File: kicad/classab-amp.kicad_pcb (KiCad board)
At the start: 2 copper layers, 116.6 x 99.3 mm, 81 parts, among them J1 INPUT, Q1 2N5401, Q10 BD140, Q11 BD139, Q12 BD139, Q13 TTC004B, Q14 TTA004B, Q15 IRFP240, Q16 IRFP9240, Q17 IRFP9240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

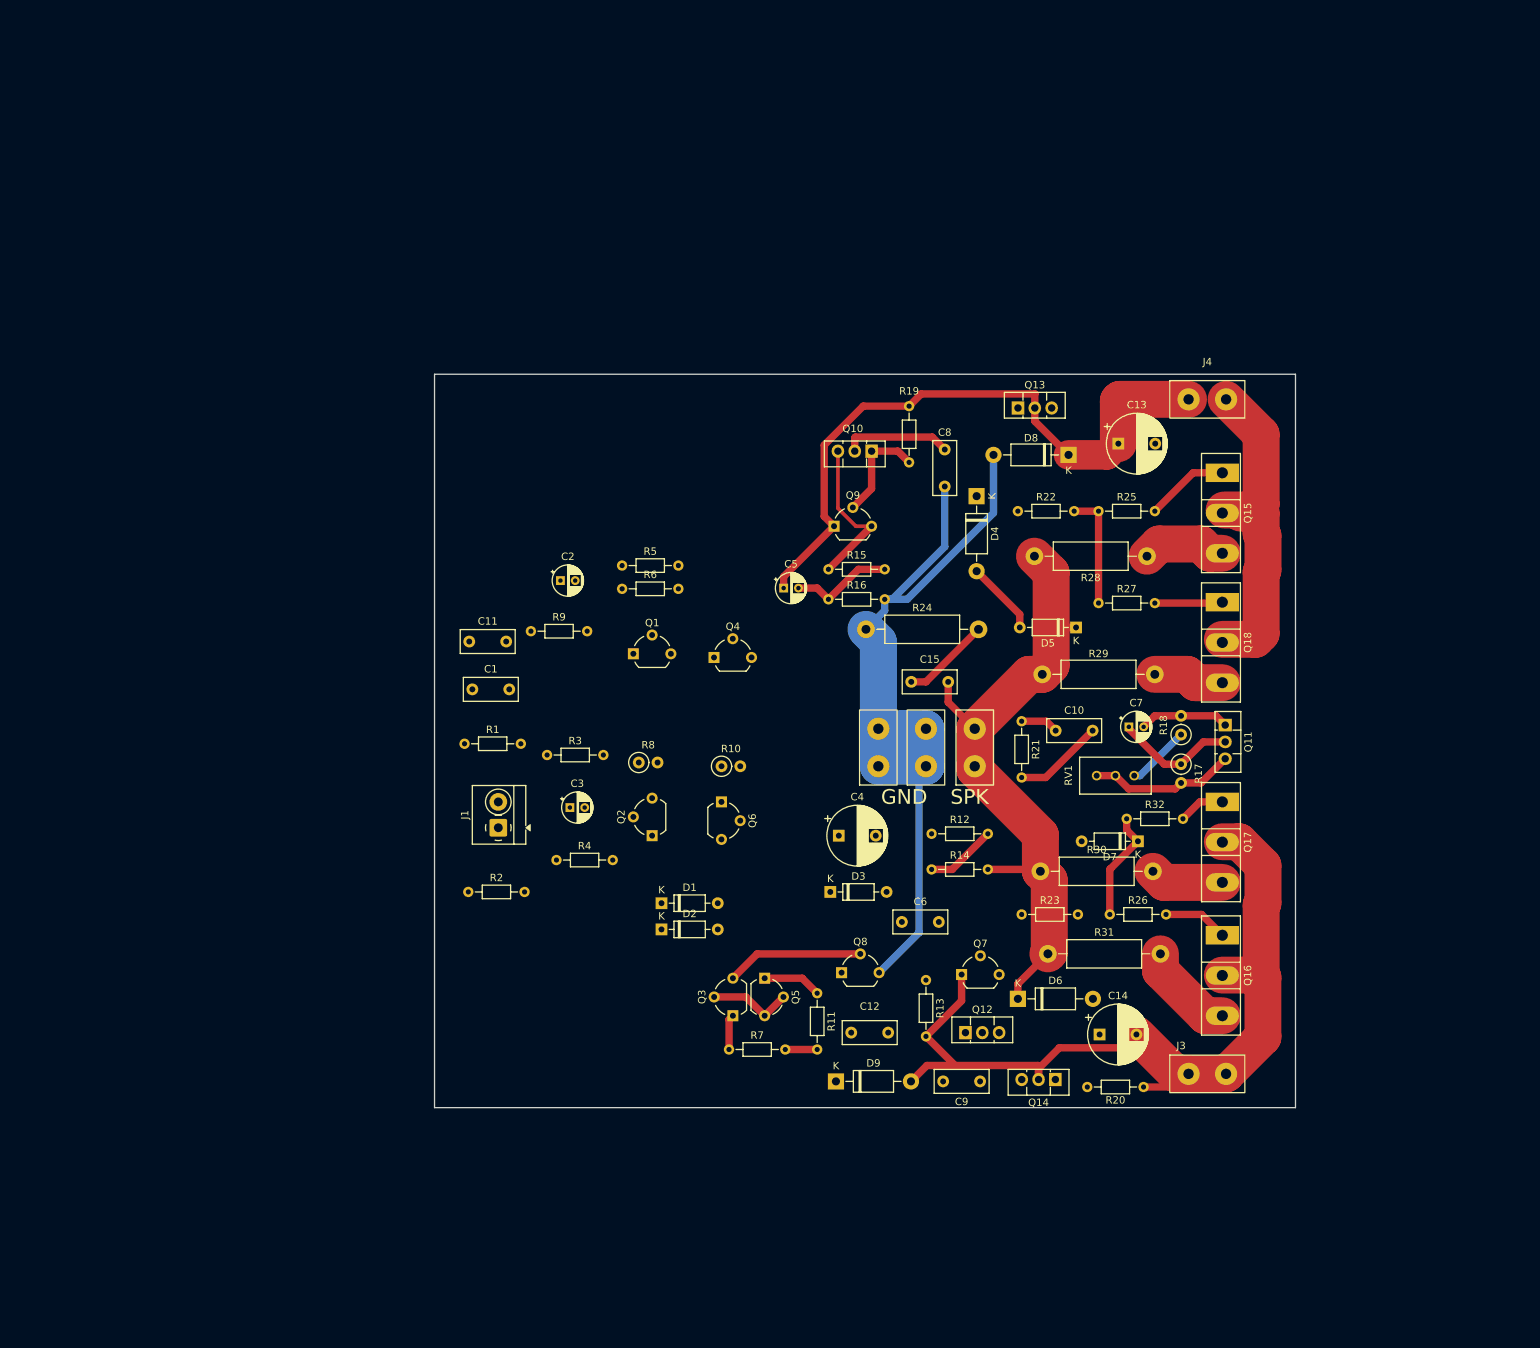
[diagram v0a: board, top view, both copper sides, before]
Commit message: Added preamp sim
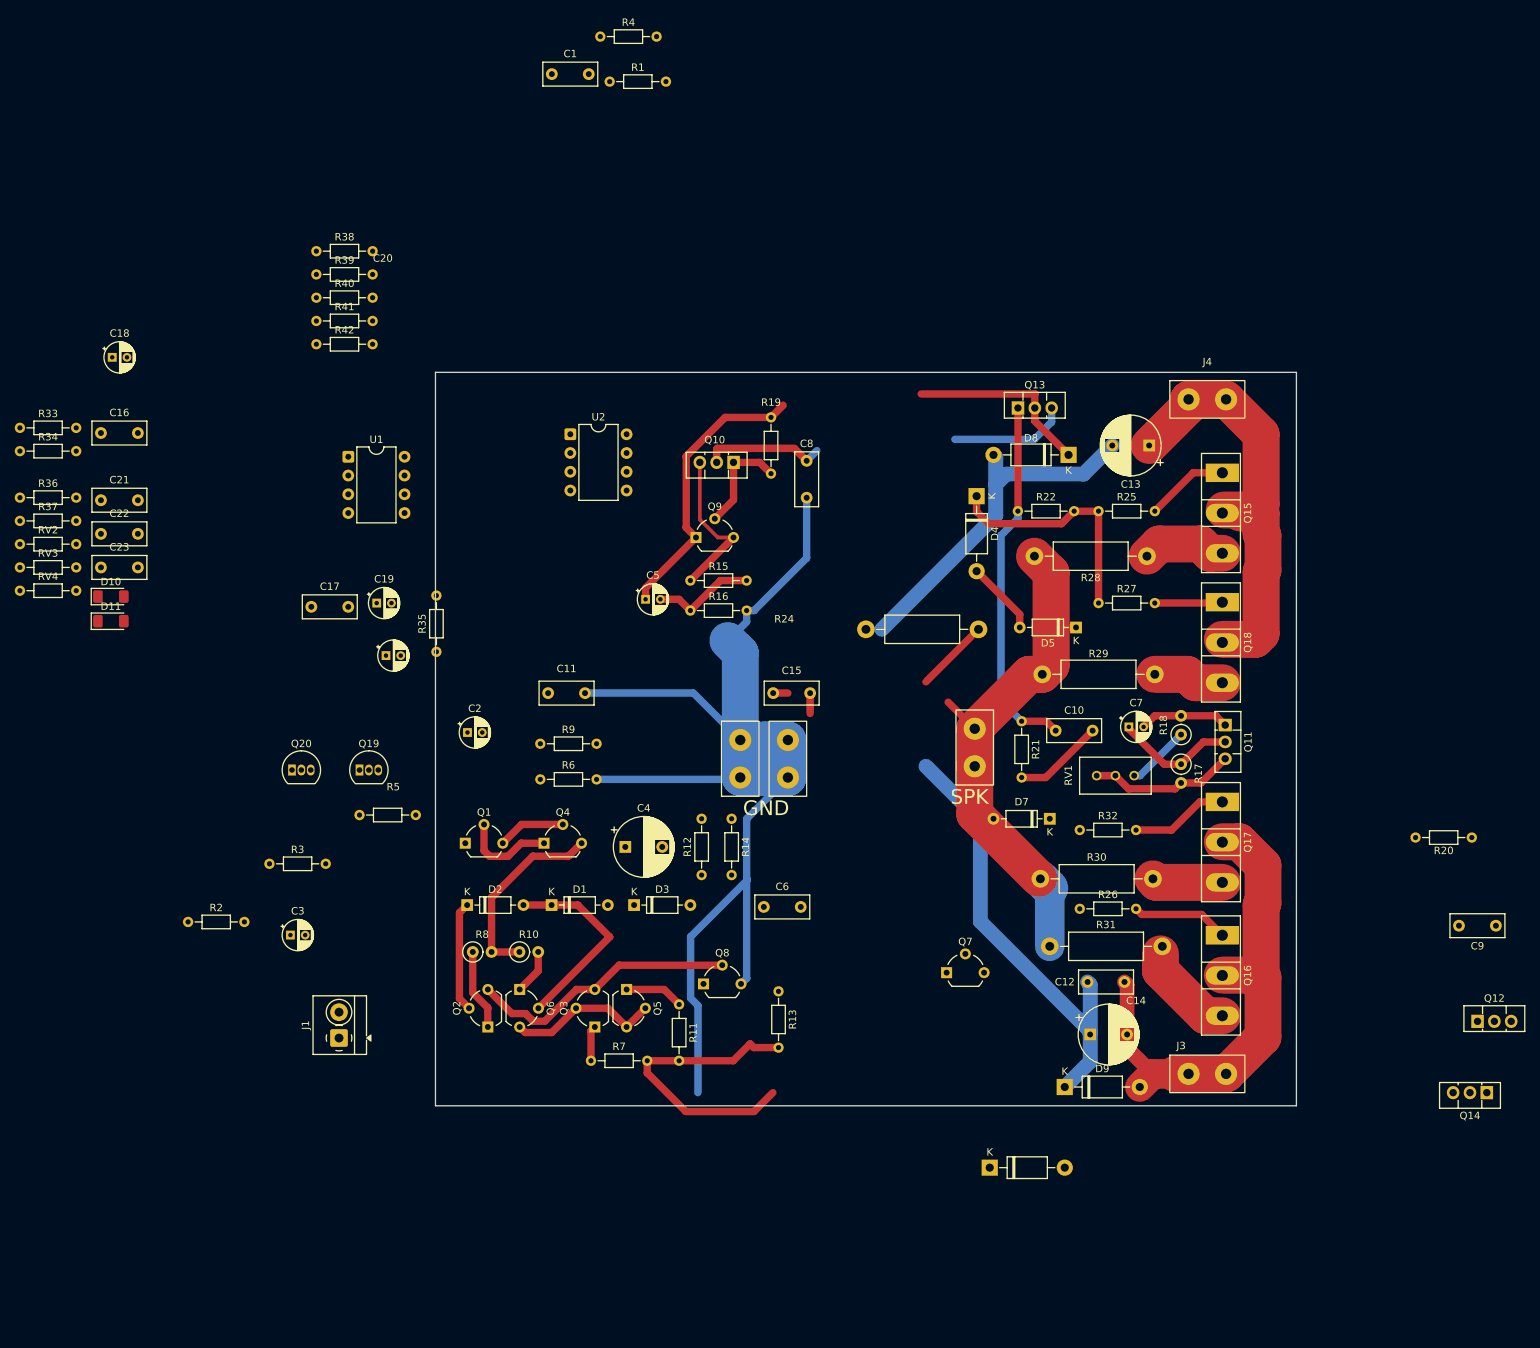
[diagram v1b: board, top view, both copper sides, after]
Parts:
- removed R23: 56, Resistor_THT:R_Axial_DIN0204_L3.6mm_D1.6mm_P7.62mm_Horizontal
- added C16: 100n, Capacitor_THT:C_Rect_L7.2mm_W3.0mm_P5.00mm_FKS2_FKP2_MKS2_MKP2, F.Cu at (45.3, 24.2)
- added C17: 100n, Capacitor_THT:C_Rect_L7.2mm_W3.0mm_P5.00mm_FKS2_FKP2_MKS2_MKP2, F.Cu at (73.7, 47.8)
- added C18: 22u, Capacitor_THT:CP_Radial_D4.0mm_P2.00mm, F.Cu at (46.8, 14.0)
- added C19: 1u, Capacitor_THT:CP_Radial_D4.0mm_P2.00mm, F.Cu at (82.6, 47.2)
- added C20: 1u, Capacitor_THT:CP_Radial_D4.0mm_P2.00mm, F.Cu at (83.9, 54.4)
- added C21: 220p, Capacitor_THT:C_Rect_L7.2mm_W3.0mm_P5.00mm_FKS2_FKP2_MKS2_MKP2, F.Cu at (45.3, 33.3)
- added C22: 100n, Capacitor_THT:C_Rect_L7.2mm_W3.0mm_P5.00mm_FKS2_FKP2_MKS2_MKP2, F.Cu at (45.3, 37.9)
- added C23: 100n, Capacitor_THT:C_Rect_L7.2mm_W3.0mm_P5.00mm_FKS2_FKP2_MKS2_MKP2, F.Cu at (45.3, 42.4)
- added D10: BZV55B16, Diode_SMD:D_MiniMELF, F.Cu at (46.6, 46.4)
- added D11: BZV55B16, Diode_SMD:D_MiniMELF, F.Cu at (46.6, 49.7)
- added Q19: BC547, Package_TO_SOT_THT:TO-92_Inline, F.Cu at (80.3, 69.8)
- added Q20: BC557, Package_TO_SOT_THT:TO-92_Inline, F.Cu at (71.1, 69.8)
- added R33: 22k, Resistor_THT:R_Axial_DIN0204_L3.6mm_D1.6mm_P7.62mm_Horizontal, F.Cu at (34.3, 23.5)
- added R34: 47k, Resistor_THT:R_Axial_DIN0204_L3.6mm_D1.6mm_P7.62mm_Horizontal, F.Cu at (34.3, 26.7)
- added R35: 47k, Resistor_THT:R_Axial_DIN0204_L3.6mm_D1.6mm_P7.62mm_Horizontal, F.Cu at (90.7, 53.8)
- added R36: 3k, Resistor_THT:R_Axial_DIN0204_L3.6mm_D1.6mm_P7.62mm_Horizontal, F.Cu at (34.3, 33.0)
- added R37: 10k, Resistor_THT:R_Axial_DIN0204_L3.6mm_D1.6mm_P7.62mm_Horizontal, F.Cu at (34.3, 36.1)
- added R38: 22k, Resistor_THT:R_Axial_DIN0204_L3.6mm_D1.6mm_P7.62mm_Horizontal, F.Cu at (74.4, -0.41)
- added R39: 10k, Resistor_THT:R_Axial_DIN0204_L3.6mm_D1.6mm_P7.62mm_Horizontal, F.Cu at (74.4, 2.74)
- added R40: 10k, Resistor_THT:R_Axial_DIN0204_L3.6mm_D1.6mm_P7.62mm_Horizontal, F.Cu at (74.4, 5.89)
- added R41: 10k, Resistor_THT:R_Axial_DIN0204_L3.6mm_D1.6mm_P7.62mm_Horizontal, F.Cu at (74.4, 9.04)
- added R42: 10k, Resistor_THT:R_Axial_DIN0204_L3.6mm_D1.6mm_P7.62mm_Horizontal, F.Cu at (74.4, 12.2)
- added RV2: 50k, Resistor_THT:R_Axial_DIN0204_L3.6mm_D1.6mm_P7.62mm_Horizontal, F.Cu at (34.3, 39.3)
- added RV3: 50k, Resistor_THT:R_Axial_DIN0204_L3.6mm_D1.6mm_P7.62mm_Horizontal, F.Cu at (34.3, 42.4)
- added RV4: 50k, Resistor_THT:R_Axial_DIN0204_L3.6mm_D1.6mm_P7.62mm_Horizontal, F.Cu at (34.3, 45.6)
- added U1: NE5532, Package_DIP:DIP-8_W7.62mm, F.Cu at (78.7, 27.4)
- added U2: NE5532, Package_DIP:DIP-8_W7.62mm, F.Cu at (108.8, 24.4)
- moved R4 111.7 mm to (112.9, -29.5)
- moved R1 91.8 mm to (114.1, -23.4)
- moved C1 84.0 mm to (106.3, -24.4)
- moved C9 73.0 mm to (234.1, 90.9)
- moved Q12 69.4 mm to (231.7, 103.9)
- moved Q14 58.4 mm to (232.9, 113.5)
- moved R20 55.8 mm to (223.3, 79.0)
- moved R5 49.0 mm to (80.3, 75.9)
- moved C3 41.6 mm to (70.9, 92.2)
- moved R3 40.4 mm to (68.1, 82.5)
- moved R2 38.2 mm to (57.1, 90.4)
- moved Q6 37.3 mm to (102.0, 99.6)
- moved R10 37.2 mm to (101.9, 94.5)
- moved J1 35.7 mm to (77.5, 106.1)
- moved Q1 34.3 mm to (94.6, 79.8)
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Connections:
- C1 pad 1: Net-(J2-Pin_3) -> Net-(C1-Pad1)
- D6 pad 1: /SPEAKER -> Net-(D6-K)
- D7 pad 1: Net-(D7-K) -> Net-(D6-K)
- D7 pad 2: Net-(D6-A) -> /SPEAKER
- R1 pad 1: Net-(J2-Pin_3) -> Net-(C1-Pad1)
- R26 pad 1: Net-(D7-K) -> Net-(D6-A)
- R3 pad 1: Net-(J2-Pin_2) -> Net-(C1-Pad1)
- R32 pad 1: Net-(D7-K) -> Net-(D6-A)
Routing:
- net PWRGND: track 128.2 -> 296.3 mm
- net Net-(Q13-E): track 5.14 -> 49.6 mm
- net Net-(Q4-C): track 0.00 -> 26.4 mm
- net Net-(Q2-C): track 18.6 -> 36.7 mm
- net Net-(Q10-C): track 31.5 -> 49.2 mm
- net Net-(D1-K): track 9.62 -> 27.1 mm
- net Net-(D4-K): track 15.7 -> 32.4 mm
- net /SPEAKER: track 90.6 -> 74.4 mm
- net Net-(D7-K): track 15.2 -> 0.00 mm
- net Net-(D1-A): track 0.00 -> 14.9 mm
- net Net-(Q1-B): track 0.00 -> 12.7 mm
- net Net-(Q2-E): track 0.00 -> 11.0 mm
- net B-: track 120.7 -> 109.9 mm
- net Net-(Q3-B): track 11.5 -> 20.8 mm
- net B+: track 133.4 -> 124.2 mm
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
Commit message: WIP
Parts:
- removed C16, C17, C22, C23: 100n, Capacitor_THT:C_Rect_L7.2mm_W3.0mm_P5.00mm_FKS2_FKP2_MKS2_MKP2
- removed C18: 22u, Capacitor_THT:CP_Radial_D4.0mm_P2.00mm
- removed C19, C20: 1u, Capacitor_THT:CP_Radial_D4.0mm_P2.00mm
- removed C21: 220p, Capacitor_THT:C_Rect_L7.2mm_W3.0mm_P5.00mm_FKS2_FKP2_MKS2_MKP2
- removed D10, D11: BZV55B16, Diode_SMD:D_MiniMELF
- removed Q19: BC547, Package_TO_SOT_THT:TO-92_Inline
- removed Q20: BC557, Package_TO_SOT_THT:TO-92_Inline
- removed R33, R38: 22k, Resistor_THT:R_Axial_DIN0204_L3.6mm_D1.6mm_P7.62mm_Horizontal
- removed R34, R35: 47k, Resistor_THT:R_Axial_DIN0204_L3.6mm_D1.6mm_P7.62mm_Horizontal
- removed R36: 3k, Resistor_THT:R_Axial_DIN0204_L3.6mm_D1.6mm_P7.62mm_Horizontal
- removed R37, R39, R40, R41, R42: 10k, Resistor_THT:R_Axial_DIN0204_L3.6mm_D1.6mm_P7.62mm_Horizontal
- removed RV2, RV3, RV4: 50k, Resistor_THT:R_Axial_DIN0204_L3.6mm_D1.6mm_P7.62mm_Horizontal
- removed U1, U2: NE5532, Package_DIP:DIP-8_W7.62mm
- added C24: 100u, Capacitor_THT:CP_Radial_D4.0mm_P2.00mm, F.Cu at (145.1, 11.9)
- added C25: 100u, Capacitor_THT:CP_Radial_D4.0mm_P2.00mm, F.Cu at (145.6, 129.3)
- added C26: 100p, Capacitor_THT:C_Rect_L7.2mm_W3.0mm_P5.00mm_FKS2_FKP2_MKS2_MKP2, F.Cu at (135.7, 100.1)
- added G***: LOGO, footprints:cyclist, F.Cu at (107.7, 32.0)
- added H1: MountingHole, MountingHole:MountingHole_3.2mm_M3, F.Cu at (96.0, -2.54)
- added H2: MountingHole, MountingHole:MountingHole_3.2mm_M3, F.Cu at (202.2, -2.54)
- added H3: MountingHole, MountingHole:MountingHole_3.2mm_M3, F.Cu at (202.2, 142.0)
- added H4: MountingHole, MountingHole:MountingHole_3.2mm_M3, F.Cu at (96.0, 142.2)
- added R23: 56, Resistor_THT:R_Axial_DIN0204_L3.6mm_D1.6mm_P7.62mm_Horizontal, F.Cu at (163.2, 115.6)
- added R43: 100, Resistor_THT:R_Axial_DIN0207_L6.3mm_D2.5mm_P10.16mm_Horizontal, F.Cu at (157.7, 11.9)
- added R44: 100, Resistor_THT:R_Axial_DIN0207_L6.3mm_D2.5mm_P10.16mm_Horizontal, F.Cu at (152.9, 129.8)
- added R45: 2.2k, Resistor_THT:R_Axial_DIN0204_L3.6mm_D1.6mm_P7.62mm_Horizontal, F.Cu at (159.5, 90.4)
- added R46: 2.2k, Resistor_THT:R_Axial_DIN0204_L3.6mm_D1.6mm_P7.62mm_Horizontal, F.Cu at (151.9, 95.2)
- C6: value 47p -> 100p
- R10, R8: footprint Resistor_THT:R_Axial_DIN0207_L6.3mm_D2.5mm_P2.54mm_Vertical -> Resistor_THT:R_Axial_DIN0204_L3.6mm_D1.6mm_P7.62mm_Horizontal
- moved R1 139.9 mm to (106.2, 116.3)
- moved C1 132.8 mm to (107.5, 108.5)
- moved R4 131.2 mm to (106.2, 101.6)
- moved Q12 84.9 mm to (147.6, 115.6), turned to 180 degrees
- moved C11 83.6 mm to (185.4, 21.8), turned to 0 degrees
- moved R20 80.0 mm to (151.8, 114.9)
- moved R2 71.7 mm to (128.8, 90.4), turned to 180 degrees
- moved C9 70.5 mm to (164.4, 101.3)
- moved Q14 68.6 mm to (164.5, 108.6)
- moved R5 62.0 mm to (129.8, 38.6), turned to 180 degrees
- moved C2 48.3 mm to (135.6, 38.9), turned to 180 degrees
- moved R6 41.9 mm to (122.2, 33.0)
- moved D7 39.8 mm to (175.3, 116.2), turned to 90 degrees
- moved R3 38.8 mm to (106.2, 89.9)
- moved Q1 38.6 mm to (123.2, 53.9)
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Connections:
- C2 pad 1: B+ -> /LP+
- C5 pad 1: B+ -> /LP+
- C6 pad 1: Net-(Q2-C) -> Net-(C26-Pad2)
- Q1 pad 1: B+ -> /LP+
- Q15 pad 1: Net-(Q15-G) -> B+
- Q7 pad 1: B- -> /LP-
- Q9 pad 1: B+ -> /LP+
- R11 pad 2: B- -> /LP-
- R13 pad 2: B- -> /LP-
- R19 pad 1: B+ -> /LP+
- R20 pad 2: B- -> /LP-
- R25 pad 2: Net-(Q15-G) -> B+
- R7 pad 2: B- -> /LP-
- R9 pad 1: B+ -> /LP+
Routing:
- net PWRGND: track 296.3 -> 626.6 mm
- net Net-(Q11-E): track 12.2 -> 120.2 mm
- net /LP+: track 0.00 -> 90.7 mm
- net GNDS: track 0.00 -> 77.3 mm
- net /LP-: track 0.00 -> 69.8 mm
- net Net-(D6-A): track 0.00 -> 64.6 mm
- net /SPEAKER: track 74.4 -> 125.6 mm
- net Net-(Q10-C): track 49.2 -> 98.7 mm
- net Net-(Q14-E): track 12.2 -> 54.6 mm
- net Net-(Q2-C): track 36.7 -> 78.5 mm
- net B-: track 109.9 -> 147.1 mm
- net Net-(C1-Pad1): track 0.00 -> 28.5 mm
- net Net-(D4-K): track 32.4 -> 58.1 mm
- net Net-(C26-Pad2): track 0.00 -> 25.1 mm
- net Net-(Q10-B): track 21.6 -> 43.5 mm
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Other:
- board size 116.6 x 99.3 mm -> 113.5 x 152.5 mm
- board text added: "B+"
- board text added: "B-"
- board text added: "IN"
- board text added: "It never gets easier, you just go faster."
- board text added: "https://github.com/prydin/bog-on-a-plate"

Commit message: WIP
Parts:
- removed the G*** at (107.7, 32.0)
- added G***: LOGO, footprints:logo, F.Cu at (105.9, 18.5)
- moved Q13 6.47 mm to (161.0, 33.1)
- moved R22 4.83 mm to (159.4, 39.1)
- moved C8 4.35 mm to (165.8, 22.1)
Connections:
- Q15 pad 1: B+ -> Net-(Q15-G)
- R25 pad 2: B+ -> Net-(Q15-G)
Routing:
- net PWRGND: track 626.6 -> 937.4 mm
- net Net-(Q13-E): track 50.6 -> 44.4 mm
- net Net-(Q15-G): track 0.00 -> 5.09 mm
- net Net-(D4-K): track 58.1 -> 62.0 mm
- net Net-(Q10-C): track 98.7 -> 101.6 mm
- net B+: track 145.3 -> 147.5 mm
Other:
- board text added: "200W V1.0"
- board text removed: "It never gets easier, you just go faster."
